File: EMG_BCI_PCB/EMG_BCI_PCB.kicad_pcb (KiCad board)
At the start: 4 copper layers, 74 parts, among them J1 Conn_01x08_Pin, J2 2.54 mm header, U1 INA350, U2 ADA4807-4ARUZ, U3 ADA4807-4ARUZ, U5 MCP1727-3302xSN, U7 LM2776, U8 MCP1501-18xCH, U9 MCP3202

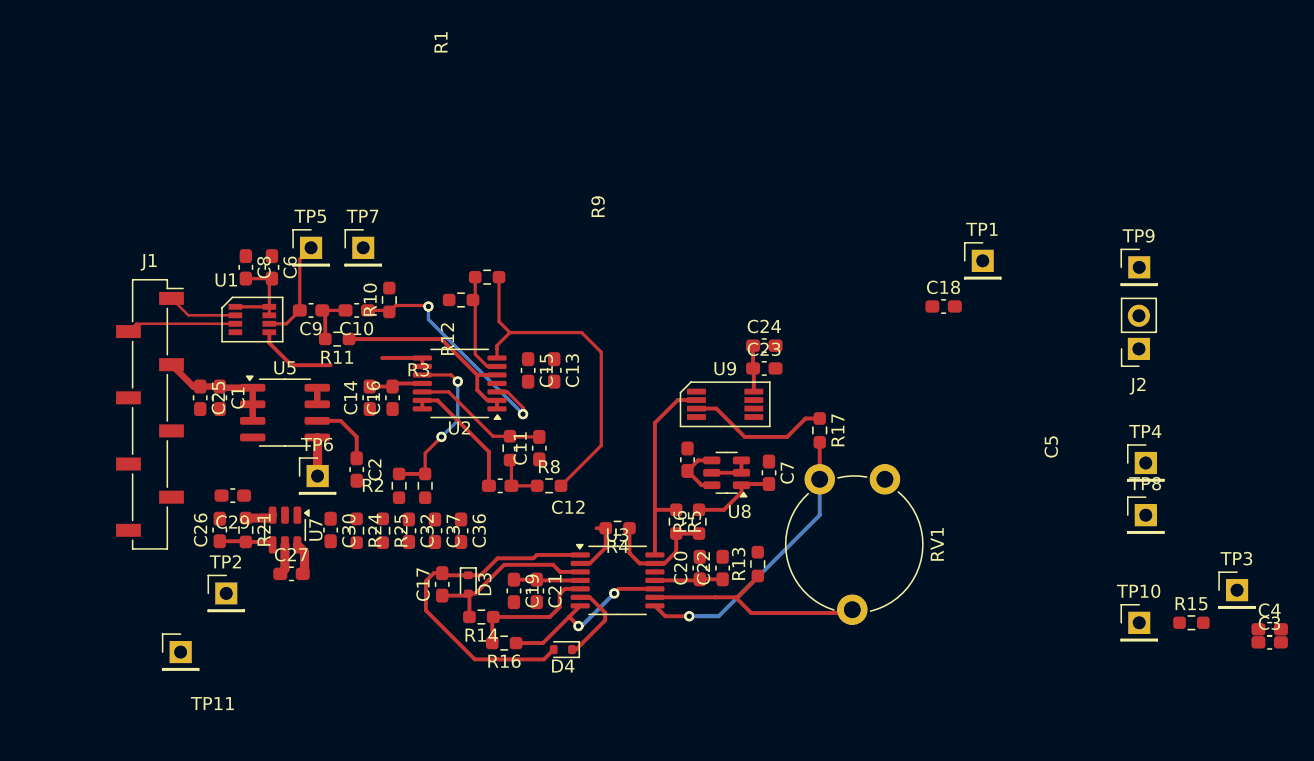
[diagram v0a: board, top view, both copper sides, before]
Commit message: Ordering the components
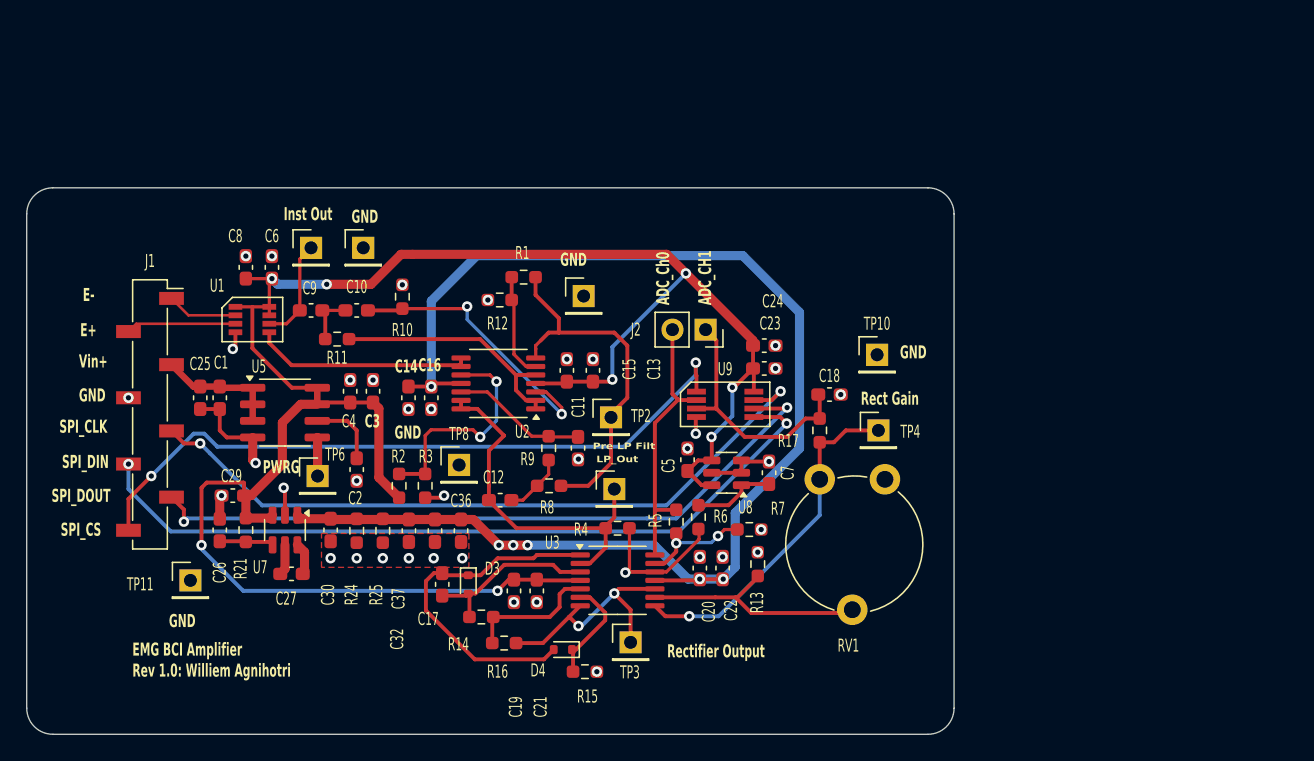
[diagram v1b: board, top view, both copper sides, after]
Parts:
- added R7: 10k, Resistor_SMD:R_0603_1608Metric_Pad0.98x0.95mm_HandSolder, F.Cu at (145.6, 106.6)
- U1: value INA350 -> INA350CDS
- moved C4 72.8 mm to (115.0, 96.0), turned to 90 degrees
- moved C3 71.4 mm to (116.8, 96.0), turned to 90 degrees
- moved TP8 52.8 mm to (123.3, 101.7)
- moved TP3 46.7 mm to (136.5, 115.2)
- moved R15 46.7 mm to (133.0, 117.5), turned to 180 degrees
- moved TP9 42.7 mm to (132.9, 88.7)
- moved J2 33.3 mm to (142.2, 91.3), turned to -90 degrees
- moved TP1 33.2 mm to (135.2, 103.5)
- moved TP2 32.4 mm to (135.0, 98.0)
- moved TP10 28.7 mm to (155.4, 93.2)
- moved TP4 20.7 mm to (155.5, 99.0)
- moved C18 11.1 mm to (151.8, 96.2)
- moved TP11 5.55 mm to (102.8, 110.5)
- moved C11 2.97 mm to (132.5, 100.4)
- moved C13 2.97 mm to (133.6, 94.4)
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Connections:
- R4 pad 1: Net-(U3D--) -> Net-(U3D-+)
- R6 pad 1: Net-(U3D--) -> Net-(U3D-+)
- U3 pad 12: Earth -> Net-(U3D-+)
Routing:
- net +3.3V: track 24.1 -> 158.9 mm, vias 0 -> 8
- net -3V3: track 9.36 -> 104.9 mm, vias 0 -> 6
- net /SPI_DIN: track 0.00 -> 59.9 mm, vias 0 -> 2
- net /SPI_CLK: track 0.00 -> 55.0 mm, vias 0 -> 2
- net /SPI_DOUT: track 0.00 -> 54.7 mm, vias 0 -> 2
- net /SPI_CS: track 0.00 -> 53.9 mm, vias 0 -> 2
- net Earth: track 3.23 -> 21.5 mm, vias 0 -> 37
- net /EMG_FrontEnd/LP_OUT: track 14.6 -> 27.3 mm
- net Net-(U3D-+): track 0.00 -> 10.7 mm, vias 0 -> 1
- net /EMG_ADC/AdcCh1: track 10.9 -> 19.2 mm
- net Net-(U1-Ref): track 9.97 -> 16.9 mm
- net /EMG_ADC/AdcCh0: track 15.7 -> 21.3 mm
- net Net-(R17-Pad2): track 21.8 -> 26.6 mm
- net Net-(U3C-+): track 14.1 -> 18.4 mm
- net Net-(U2C-+): track 13.0 -> 17.3 mm
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- added copper zone on F.Cu, net Earth
- added copper zone on In1.Cu, net Earth
- added copper zone on In2.Cu, net Earth
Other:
- board outline added: 71.1 x 41.9 mm
- rule pad_to_mask_clearance: 0.05 -> 0
- board text added: "ADC_Ch0 ADC_CH1"
- board text added: "E+"
- board text added: "E-"
- board text added: "EMG BCI Amplifier Rev 1.0: Williem Agnihotri"
- board text added: "GND"
- board text added: "Inst Out"
- board text added: "LP_Out"
- board text added: "PWRG"
- board text added: "Pre LP Filt"
- board text added: "Rect Gain"
- board text added: "Rectifier Output"
- board text added: "SPI_CLK"
- board text added: "SPI_CS"
- board text added: "SPI_DIN"
- board text added: "SPI_DOUT"
- board text added: "Vin+"

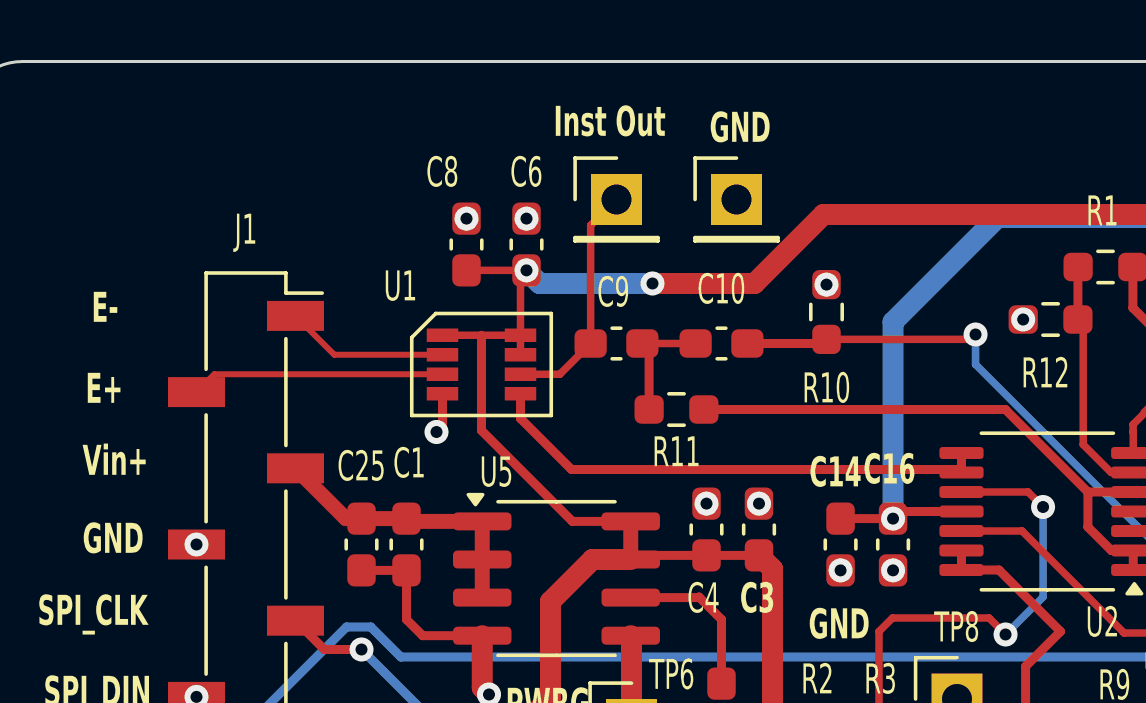
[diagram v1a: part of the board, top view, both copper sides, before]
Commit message: Adjusts PCB and schematic with changes
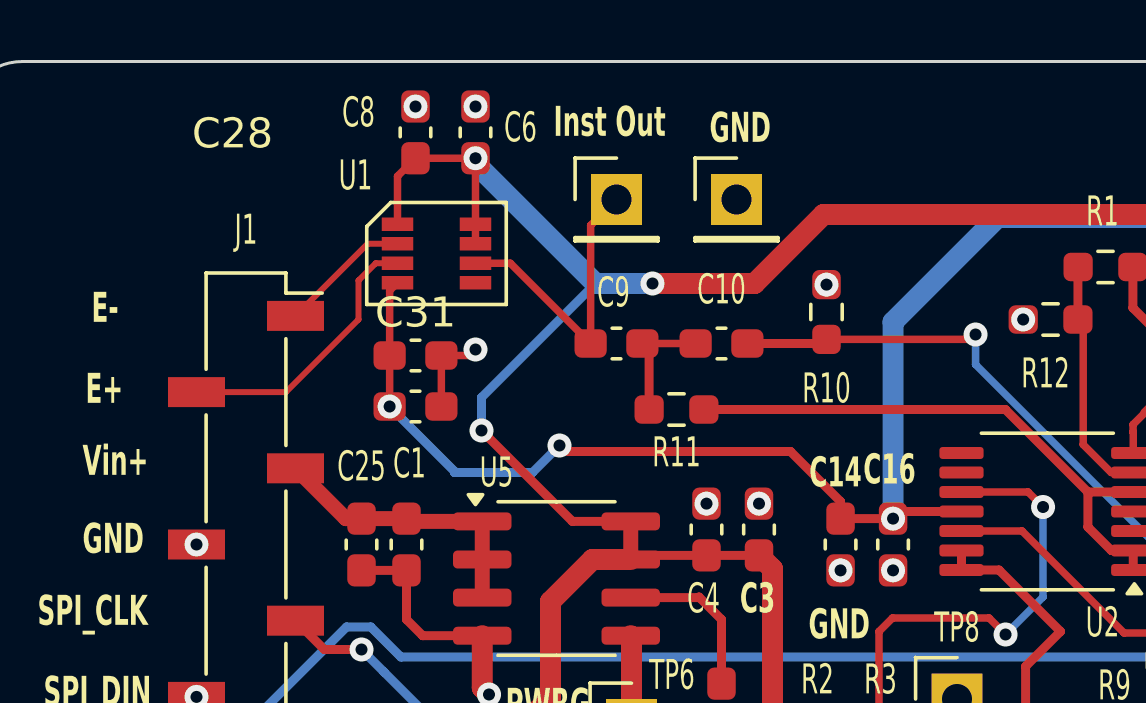
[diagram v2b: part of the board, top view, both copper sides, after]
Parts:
- added C28: 4.7uF, Capacitor_SMD:C_0603_1608Metric_Pad1.08x0.95mm_HandSolder, F.Cu at (105.3, 91.9)
- added C31: 0.1uF, Capacitor_SMD:C_0603_1608Metric_Pad1.08x0.95mm_HandSolder, F.Cu at (105.3, 90.2)
- moved C6 4.11 mm to (107.3, 82.8)
- moved C8 4.11 mm to (105.3, 82.8)
- moved U1 3.99 mm to (106.0, 86.8)
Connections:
- C17 pad 1: Net-(D3-A) -> Net-(D3-K)
- C17 pad 2: Net-(D3-K) -> Net-(D3-A)
- R14 pad 1: Net-(U3B-+) -> Net-(U3B--)
- R16 pad 2: Net-(U3B-+) -> Net-(U3B--)
- R4 pad 2: /EMG_FrontEnd/LP_OUT -> unconnected-(R4-Pad2)
- U1 pad 4: Earth -> -3V3
- U1 pad 5: Net-(U1-Ref) -> unconnected-(U1-Ref-Pad5)
- U2 pad 10: Net-(U2C-+) -> (no net)
- U2 pad 8: Net-(U1-Ref) -> (no net)
- U2 pad 9: Net-(U1-Ref) -> (no net)
- U3 pad 2: /EMG_FrontEnd/LP_OUT -> Net-(D3-A)
- U3 pad 3: Net-(D3-A) -> /EMG_FrontEnd/LP_OUT
- U3 pad 5: Net-(U3B-+) -> Net-(D4-K)
- U3 pad 6: Net-(D4-K) -> Net-(U3B--)
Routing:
- net -3V3: track 104.9 -> 126.9 mm, vias 6 -> 8
- net Net-(U1-Ref): track 16.9 -> 0.00 mm
- net Net-(U3B-+): track 10.2 -> 0.00 mm
- net Net-(D4-K): track 8.19 -> 18.4 mm
- net +3.3V: track 158.9 -> 165.8 mm, vias 8 -> 9
- net Net-(C9-Pad2): track 7.92 -> 10.1 mm
- net Earth: track 21.5 -> 23.1 mm
- net /EMG_FrontEnd/Electrode-: track 5.44 -> 4.40 mm
- net /EMG_FrontEnd/Electrode+: track 8.45 -> 9.24 mm
